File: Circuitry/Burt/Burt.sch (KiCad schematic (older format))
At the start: 50 parts

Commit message: Joe: RTC changed to soic8, added labels to screw terminal, removed shift regs Burt: added shift reg
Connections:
- net labels added: +3.3V, RCLK, SER, SRCLK
- net labels removed: BWL
- wire segments 118 -> 120
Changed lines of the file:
@@
 	1    0    0    -1
 $EndComp
-Text Label 4150 1800 2    50   ~ 0
-BWL
+Text Label 4675 1225 2    50   ~ 0
+IN1
+Text Label 4675 1325 2    50   ~ 0
+IN2
 Text Label 4550 4450 2    50   ~ 0
-BWL
-Text Label 4150 1900 2    50   ~ 0
-IN1
-Text Label 4150 2000 2    50   ~ 0
-IN2
+SER
+Text Label 4550 4650 2    50   ~ 0
+SRCLK
+Text Label 4550 4950 2    50   ~ 0
+RCLK
+Text Label 5350 4450 0    50   ~ 0
+BL1
+Text Label 5350 4550 0    50   ~ 0
+BL1
+Text Label 5350 4650 0    50   ~ 0
+BL1
+Text Label 5350 4750 0    50   ~ 0
+BL1
+Text Label 5350 4850 0    50   ~ 0
+BL1
+Text Label 5350 4950 0    50   ~ 0
+BL1
+Text Label 5350 5050 0    50   ~ 0
+BL1
+Text Label 5350 5150 0    50   ~ 0
+BL1
+$Comp
+L power:GND #PWR?
+U 1 1 5D2A6513
+P 4175 5050
+F 0 "#PWR?" H 4175 4800 50  0001 C CNN
+F 1 "GND" H 4180 4877 50  0000 C CNN
+F 2 "" H 4175 5050 50  0001 C CNN
+F 3 "" H 4175 5050 50  0001 C CNN
+	1    4175 5050
+	1    0    0    -1
+$EndComp
+Wire Wire Line
+	4175 5050 4550 5050
+Wire Wire Line
+	4175 4750 4550 4750
+$Comp
+L power:+3.3V #PWR?
+U 1 1 5D2BCF22
+P 4175 4750
+F 0 "#PWR?" H 4175 4600 50  0001 C CNN
+F 1 "+3.3V" H 4190 4923 50  0000 C CNN
+F 2 "" H 4175 4750 50  0001 C CNN
+F 3 "" H 4175 4750 50  0001 C CNN
+	1    4175 4750
+	1    0    0    -1
+$EndComp
 $EndSCHEMATC

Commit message: Added part URLs
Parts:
- removed D? (x3): LED, symbol Device:LED
- removed D?: D, symbol Device:D
- removed J?: Conn_01x05_Female, symbol Connector:Conn_01x05_Female
- removed Q? (x10): Q_NMOS_DGS, symbol Device:Q_NMOS_DGS
- removed R? (x3): R, symbol Device:R
- added D1: LED, symbol Device:LED
- added Q1, Q2, Q3, Q4, Q5: SSM6N58NU, symbol Custom:SSM6N58NU
- BT1: renamed from BT?; Part URL (none) -> https://www.digikey.com/product-detail/en/jst-sales-america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
- C1, C2: renamed from C?; Part URL (none) -> https://www.digikey.com/product-detail/en/samsung-electro-m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
- M1: renamed from M?; Part URL (none) -> https://www.pololu.com/product/4790/
- R10, R11, R12, R18, R19, R20, R21, R22, R4, R5, R8, R9: renamed from R?; Part URL (none) -> https://www.digikey.com/product-detail/en/yageo/RT0603BRD07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
- R6, R7: renamed from R?; Part URL (none) -> https://www.digikey.com/product-detail/en/yageo/RC0603FR-07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
- U1, U3: renamed from U?; Part URL (none) -> https://www.digikey.com/product-detail/en/microchip-technol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
- U2: renamed from U?; Part URL (none) -> https://www.digikey.com/product-detail/en/allegro-microsyst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
- U4: renamed from U?; Part URL (none) -> https://www.digikey.com/product-detail/en/nexperia-usa-inc/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
- gave numbers to parts that had none: 10
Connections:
- wire segments 120 -> 117
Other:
- note removed: "Programming LEDs"

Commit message: burt organization and screw terminal and image sensor connector
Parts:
- added J?: Conn_01x08_Female, symbol Connector:Conn_01x08_Female
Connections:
- net labels added: +3V3, CS, MISO, MOSI, SCL, SCLK, SDA
- net labels removed: +3.3V, RX, TX
- wire segments 117 -> 116
- no-connect marks 0 -> 1
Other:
- note added: "Burn Wire Circuitry for Launchers"
- note added: "Burn Wire Circuitry for Pyrolysis"
- note added: "Burn Wire Input 1 for Pyrolysis"
- note added: "Burn Wire Input 2 for Pyrolysis"
- note added: "CS Input for Img Sensor"
- note added: "Img Sensor Data Output"
- note added: "Input = Data from Burt to Joe\nOutput = Data from Joe to Burt"
- note added: "MISO Input for Img Sensor"
- note added: "MOSI Input for Img Sensor"
- note added: "Motor Driver for Launchers Input 1"
- note added: "Motor Driver for Launchers Input 2"
- note added: "Reg Clk Input for Shift Reg"
- note added: "SCL Input for Img Sensor"
- note added: "SCLK Input for Img Sensor"
- note added: "SDA Input for Img Sensor"
- note added: "Serial Clk Input for Shift Reg"
- note added: "Serial Input for Shift Reg"
- note added: "Temp Sensor Data Output"
- note removed: "Burt <--> Joe"
- moved on the sheet: BT1, C1, C2, D1, M1, Q1A, Q1B, Q2A, Q2B, Q3A, Q3B, Q4A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

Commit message: fixed burn wire circuits
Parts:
- removed unit 2 of Q1
- removed Q2, Q3, Q4, Q5: SSM6N58NU, symbol Custom:SSM6N58NU
- removed R10, R11, R12, R18, R19, R20, R21, R22, R9: 10k, symbol Device:R
- removed R14, R15, R16, R17, R23, R24, R25, R26, R27: BURNWIRE, symbol Device:R
- added J?: Conn_01x17, symbol Connector_Generic:Conn_01x17
- added Q? (x9): SSM6N58NU, symbol Custom:SSM6N58NU
- added R? (x9): BURNWIRE, symbol Device:R
- added R? (x9): 10k, symbol Device:R
- J?: Part URL (none) -> https://www.digikey.com/product-detail/en/sullins-connector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
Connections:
- net labels added: CS_IMG, SCK
- net labels removed: CVBS
- wire segments 116 -> 86
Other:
- note added: "Drain"
- note added: "Gate\n"
- note added: "Shift Registers for Launcher Burn Wires"
- note added: "Source"
- note removed: "Img Sensor Data Output"
- moved on the sheet: Q1A, R13, R8, U4

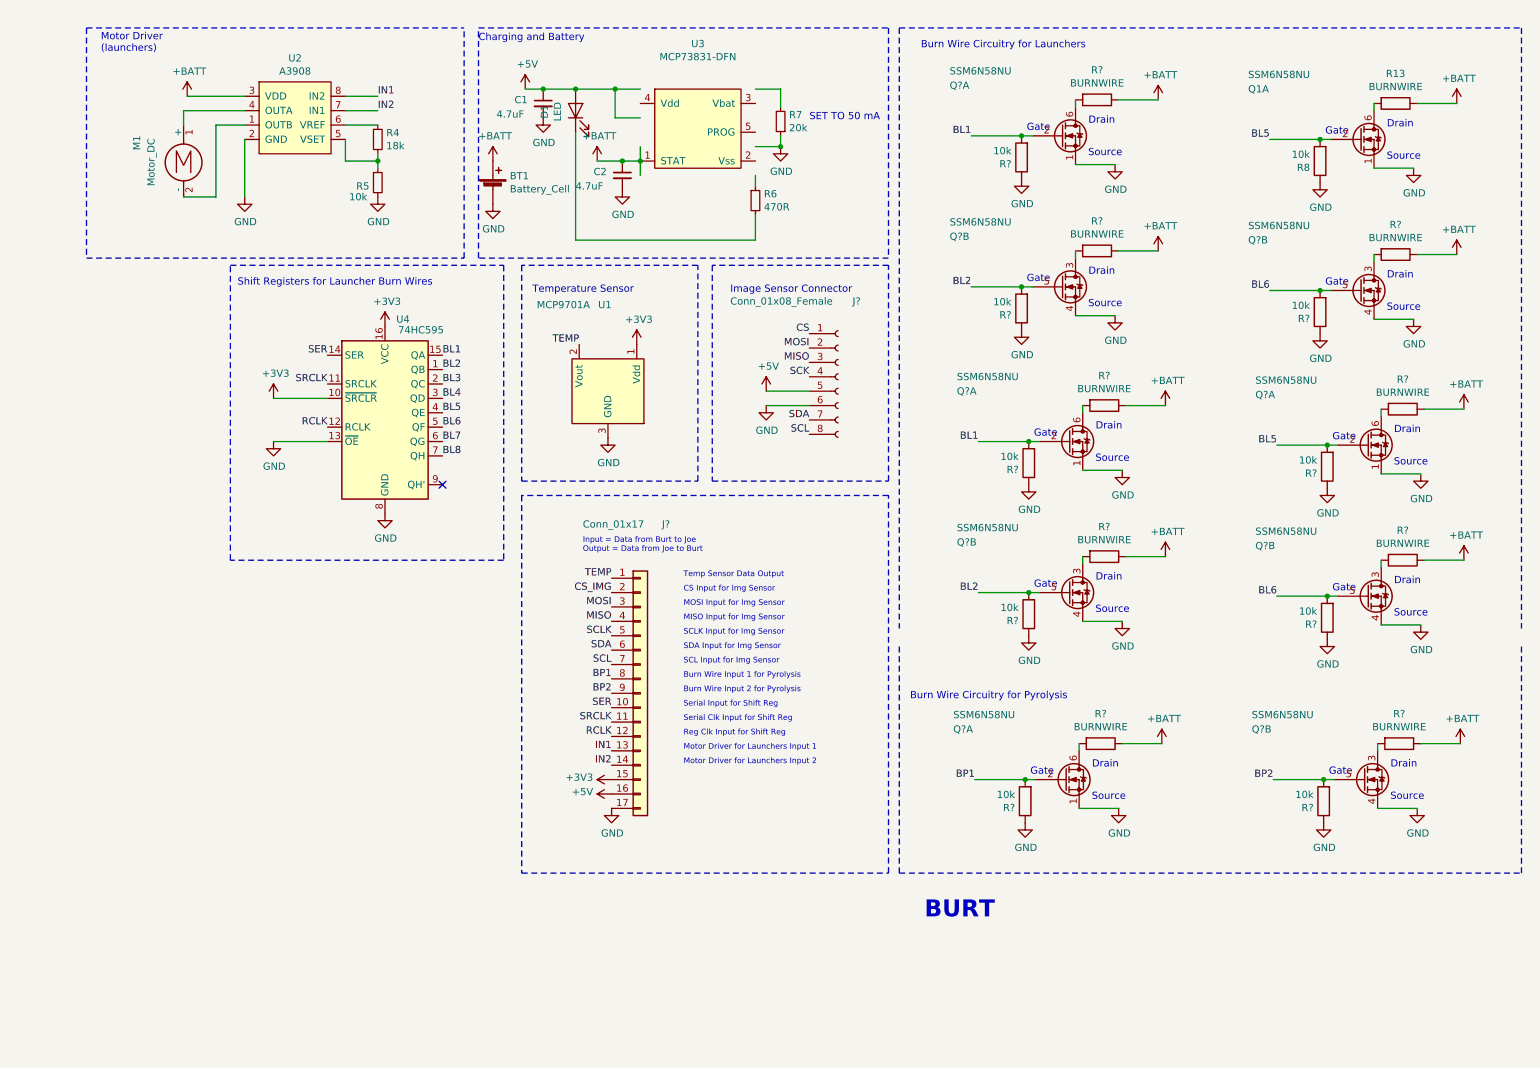
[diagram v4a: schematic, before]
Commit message: electrical rules check ran and corrected
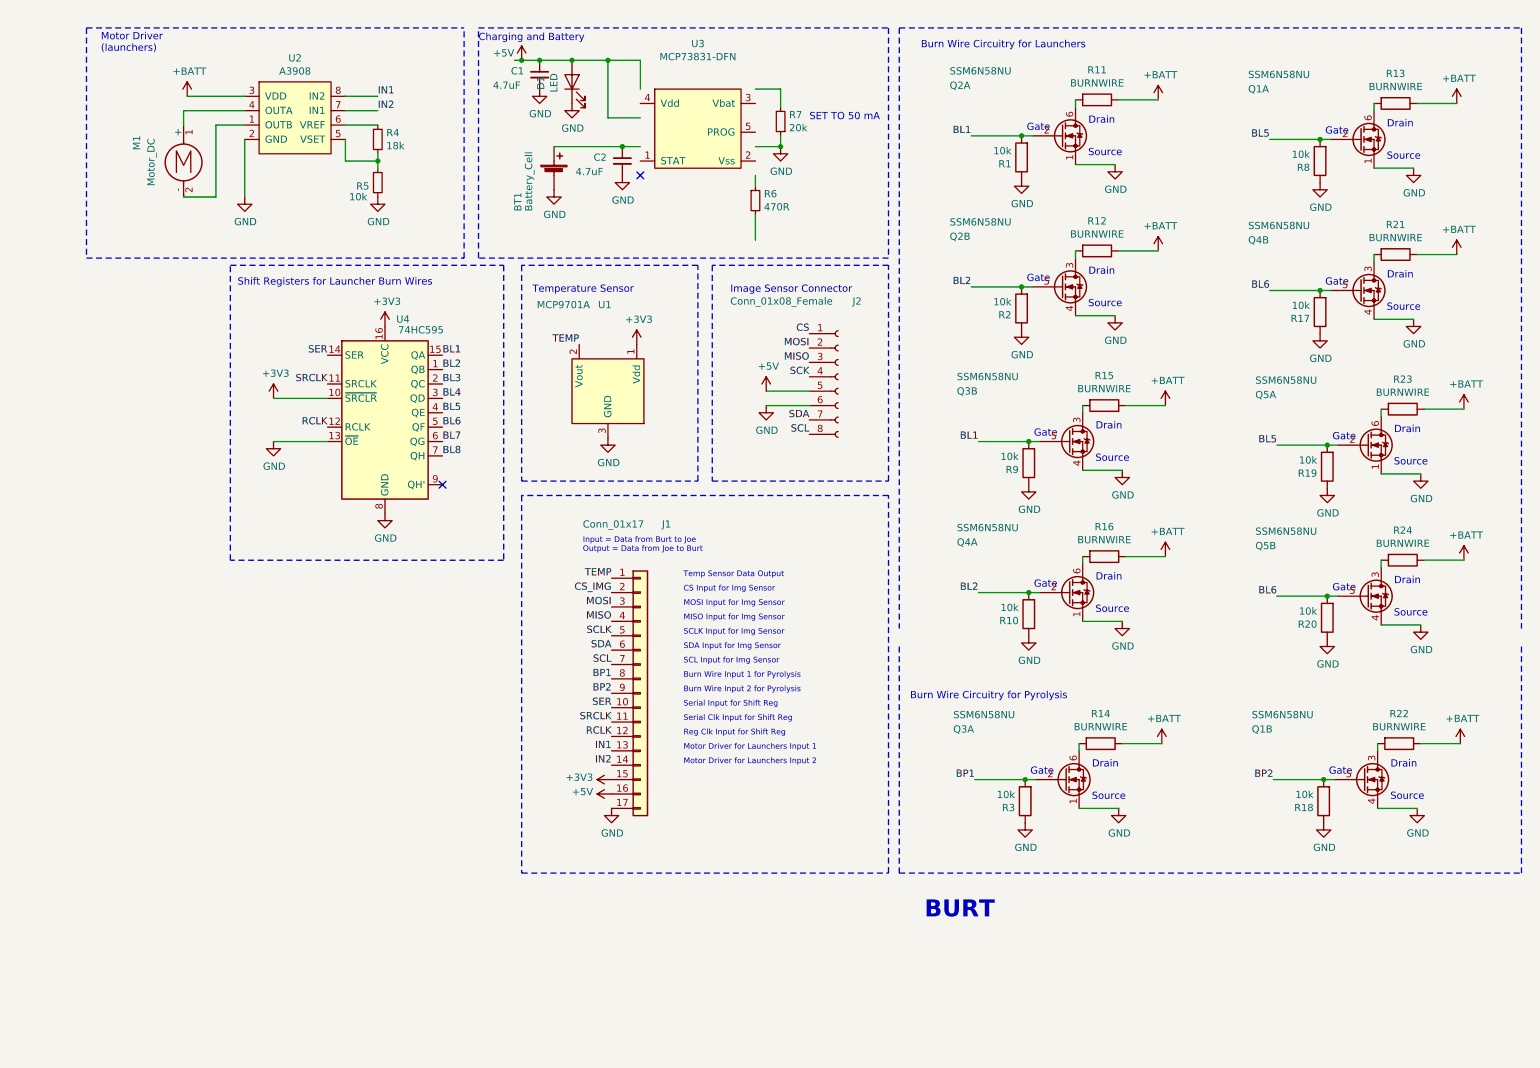
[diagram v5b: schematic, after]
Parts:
- gave numbers to parts that had none: 25
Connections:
- wire segments 86 -> 84
- no-connect marks 1 -> 2
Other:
- moved on the sheet: BT1, C1, C2, D1

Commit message: footprints for burt
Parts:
- C1, C2: footprint (none) -> Capacitor_SMD:C_0603_1608Metric
- D1: footprint (none) -> LED_SMD:LED_0201_0603Metric
- J2: footprint (none) -> Connector_PinSocket_1.00mm:PinSocket_1x08_P1.00mm_Vertical
- M1: footprint (none) -> Connector_JST:JST_JWPF_B02B-JWPF-SK-R_1x02_P2.00mm_Vertical
- Q1, Q2, Q3, Q4, Q5: footprint (none) -> Package_DFN_QFN:DFN-6-1EP_2x2mm_P0.65mm_EP1x1.6mm
- R1, R10, R17, R18, R19, R2, R20, R3, R4, R5, R6, R7, R8, R9: footprint (none) -> Resistor_SMD:R_0603_1608Metric
- R11, R12, R13, R14, R15, R16, R21, R22, R23, R24: footprint (none) -> Connector_PinHeader_1.00mm:PinHeader_1x02_P1.00mm_Vertical
- U1: footprint (none) -> Package_TO_SOT_SMD:SOT-23
- U2: footprint (none) -> Custom:A3908
- U3: footprint (none) -> Package_DFN_QFN:DFN-8-1EP_3x2mm_P0.5mm_EP1.3x1.5mm

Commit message: Fixed some garbage
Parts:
- BT1: footprint (none) -> Connector_JST:JST_PH_B2B-PH-K_1x02_P2.00mm_Vertical
- D1: footprint LED_SMD:LED_0201_0603Metric -> LED_SMD:LED_0603_1608Metric
- J1: footprint (none) -> Custom:0522071733
- J2: footprint Connector_PinSocket_1.00mm:PinSocket_1x08_P1.00mm_Vertical -> Connector_PinHeader_2.54mm:PinHeader_1x08_P2.54mm_Vertical
- M1: footprint Connector_JST:JST_JWPF_B02B-JWPF-SK-R_1x02_P2.00mm_Vertical -> Connector_JST:JST_PH_B2B-PH-K_1x02_P2.00mm_Vertical
- U3: footprint Package_DFN_QFN:DFN-8-1EP_3x2mm_P0.5mm_EP1.3x1.5mm -> Package_TO_SOT_SMD:SOT-23-5; Part URL https://www.digikey.com/product-detail/en/microchip-technology/MCP73831T-2ACI-MC/MCP73831T-2ACI-MCCT-ND/7065590 -> https://www.digikey.com/product-detail/en/microchip-technology/MCP73831T-2ACI-OT/MCP73831T-2ACI-OTCT-ND/1979802
- U4: footprint (none) -> Package_SO:SOIC-16_3.9x9.9mm_P1.27mm
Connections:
- wire segments 84 -> 82
- no-connect marks 2 -> 1
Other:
- moved on the sheet: BT1, C2, R6, R7
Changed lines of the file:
@@
 L Device:R_Small R6
 U 1 1 5D28D225
-P 5825 1750
-F 0 "R6" H 5884 1796 50  0000 L CNN
-F 1 "470R" H 5884 1705 50  0000 L CNN
-F 2 "Resistor_SMD:R_0603_1608Metric" H 5825 1750 50  0001 C CNN
-F 3 "~" H 5825 1750 50  0001 C CNN
-F 4 "https://www.digikey.com/product-detail/en/yageo/RC0603FR-07470RL/311-470HRCT-ND/730203" H 5825 1750 50  0001 C CNN "Part URL"
-	1    5825 1750
+P 4550 1175
+F 0 "R6" H 4609 1221 50  0000 L CNN
+F 1 "470R" H 4609 1130 50  0000 L CNN
+F 2 "Resistor_SMD:R_0603_1608Metric" H 4550 1175 50  0001 C CNN
+F 3 "~" H 4550 1175 50  0001 C CNN
+F 4 "https://www.digikey.com/product-detail/en/yageo/RC0603FR-07470RL/311-470HRCT-ND/730203" H 4550 1175 50  0001 C CNN "Part URL"
+	1    4550 1175
 	1    0    0    -1
 $EndComp
@@
 L Device:R_Small R7
 U 1 1 5D28D9E9
-P 6000 1200
-F 0 "R7" H 5941 1154 50  0000 R CNN
-F 1 "20k" H 5941 1245 50  0000 R CNN
-F 2 "Resistor_SMD:R_0603_1608Metric" H 6000 1200 50  0001 C CNN
-F 3 "~" H 6000 1200 50  0001 C CNN
-F 4 "https://www.digikey.com/product-detail/en/yageo/RC0603FR-0720KL/311-20.0KHRCT-ND/729987" H 6000 1200 50  0001 C CNN "Part URL"
-	1    6000 1200
+P 5925 1375
+F 0 "R7" H 5866 1329 50  0000 R CNN
+F 1 "20k" H 5866 1420 50  0000 R CNN
+F 2 "Resistor_SMD:R_0603_1608Metric" H 5925 1375 50  0001 C CNN
+F 3 "~" H 5925 1375 50  0001 C CNN
+F 4 "https://www.digikey.com/product-detail/en/yageo/RC0603FR-0720KL/311-20.0KHRCT-ND/729987" H 5925 1375 50  0001 C CNN "Part URL"
+	1    5925 1375
 	-1   0    0    1
 $EndComp
-Wire Wire Line
-	5825 975  6000 975
-Wire Wire Line
-	6000 975  6000 1100
-Wire Wire Line
-	5825 1375 6000 1375
-Wire Wire Line
-	6000 1375 6000 1300
 $Comp
 L power:GND #PWR013
 U 1 1 5D292366
-P 6000 1375
-F 0 "#PWR013" H 6000 1125 50  0001 C CNN
-F 1 "GND" H 6005 1202 50  0000 C CNN
-F 2 "" H 6000 1375 50  0001 C CNN
-F 3 "" H 6000 1375 50  0001 C CNN
-	1    6000 1375
-	1    0    0    -1
-$EndComp
-Connection ~ 6000 1375
-Wire Wire Line
-	5825 1575 5825 1650
-Wire Wire Line
-	5825 2025 5825 1850
+P 5925 1525
+F 0 "#PWR013" H 5925 1275 50  0001 C CNN
+F 1 "GND" H 5930 1352 50  0000 C CNN
+F 2 "" H 5925 1525 50  0001 C CNN
+F 3 "" H 5925 1525 50  0001 C CNN
+	1    5925 1525
+	1    0    0    -1
+$EndComp
 Text Label 4825 5075 2    50   ~ 0
 BP1
@@
 Text Label 9400 1325 2    50   ~ 0
 BL5
-Wire Wire Line
-	5025 1375 4900 1375
 $Comp
 L Burt-rescue:A3908-Custom U2
@@
 F 0 "M1" V 1525 1450 50  0000 L CNN
 F 1 "Motor_DC" V 1625 1200 50  0000 L CNN
-F 2 "Connector_JST:JST_JWPF_B02B-JWPF-SK-R_1x02_P2.00mm_Vertical" H 1850 1335 50  0001 C CNN
+F 2 "Connector_JST:JST_PH_B2B-PH-K_1x02_P2.00mm_Vertical" H 1850 1335 50  0001 C CNN
 F 3 "~" H 1850 1335 50  0001 C CNN
 F 4 "https://www.pololu.com/product/4790/" H 1850 1425 50  0001 C CNN "Part URL"
@@
 F 0 "U3" H 5425 1890 50  0000 C CNN
 F 1 "MCP73831-DFN" H 5425 1799 50  0000 C CNN
-F 2 "Package_DFN_QFN:DFN-8-1EP_3x2mm_P0.5mm_EP1.3x1.5mm" H 5425 1275 50  0001 C CNN
+F 2 "Package_TO_SOT_SMD:SOT-23-5" H 5425 1275 50  0001 C CNN
 F 3 "" H 5425 1275 50  0001 C CNN
-F 4 "https://www.digikey.com/product-detail/en/microchip-technology/MCP73831T-2ACI-MC/MCP73831T-2ACI-MCCT-ND/7065590" H 5425 1275 50  0001 C CNN "Part URL"
+F 4 "https://www.digikey.com/product-detail/en/microchip-technology/MCP73831T-2ACI-OT/MCP73831T-2ACI-OTCT-ND/1979802" H 5425 1275 50  0001 C CNN "Part URL"
 	1    5425 1275
 	1    0    0    -1
@@
 L Device:C_Small C2
 U 1 1 5D28C167
-P 4900 1475
-F 0 "C2" H 4700 1500 50  0000 L CNN
-F 1 "4.7uF" H 4575 1400 50  0000 L CNN
-F 2 "Capacitor_SMD:C_0603_1608Metric" H 4900 1475 50  0001 C CNN
-F 3 "~" H 4900 1475 50  0001 C CNN
-F 4 "https://www.digikey.com/product-detail/en/samsung-electro-mechanics/CL10A475MQ8NNNC/1276-1907-1-ND/3889993" H 4900 1475 50  0001 C CNN "Part URL"
-	1    4900 1475
-	1    0    0    -1
-$EndComp
-Connection ~ 4900 1375
-$Comp
-L power:GND #PWR09
-U 1 1 5D28CAB7
-P 4900 1575
-F 0 "#PWR09" H 4900 1325 50  0001 C CNN
-F 1 "GND" H 4905 1402 50  0000 C CNN
-F 2 "" H 4900 1575 50  0001 C CNN
-F 3 "" H 4900 1575 50  0001 C CNN
-	1    4900 1575
-	1    0    0    -1
-$EndComp
-Text Notes 6200 1200 0    50   ~ 0
+P 6225 1175
+F 0 "C2" H 6025 1200 50  0000 L CNN
+F 1 "4.7uF" H 5900 1100 50  0000 L CNN
+F 2 "Capacitor_SMD:C_0603_1608Metric" H 6225 1175 50  0001 C CNN
+F 3 "~" H 6225 1175 50  0001 C CNN
+F 4 "https://www.digikey.com/product-detail/en/samsung-electro-mechanics/CL10A475MQ8NNNC/1276-1907-1-ND/3889993" H 6225 1175 50  0001 C CNN "Part URL"
+	1    6225 1175
+	1    0    0    -1
+$EndComp
+Text Notes 6000 1600 0    50   ~ 0
 SET TO 50 mA
-$Comp
-L Device:Battery_Cell BT1
-U 1 1 5D28E83B
-P 4425 1575
-F 0 "BT1" V 4175 1325 50  0000 L CNN
-F 1 "Battery_Cell" V 4250 1325 50  0000 L CNN
-F 2 "" V 4425 1635 50  0001 C CNN
-F 3 "~" V 4425 1635 50  0001 C CNN
-F 4 "https://www.digikey.com/product-detail/en/jst-sales-america-inc/B2B-PH-K-S-LF-SN/455-1704-ND/926611" H 4425 1575 50  0001 C CNN "Part URL"
-	1    4425 1575
-	1    0    0    -1
-$EndComp
 $Comp
 L power:GND #PWR02
 U 1 1 5D291472
-P 4425 1675
-F 0 "#PWR02" H 4425 1425 50  0001 C CNN
-F 1 "GND" H 4430 1502 50  0000 C CNN
-F 2 "" H 4425 1675 50  0001 C CNN
-F 3 "" H 4425 1675 50  0001 C CNN
-	1    4425 1675
+P 6325 1375
+F 0 "#PWR02" H 6325 1125 50  0001 C CNN
+F 1 "GND" H 6450 1300 50  0000 C CNN
+F 2 "" H 6325 1375 50  0001 C CNN
+F 3 "" H 6325 1375 50  0001 C CNN
+	1    6325 1375
 	1    0    0    -1
 $EndComp
@@
 F 0 "U4" H 3375 3875 50  0000 C CNN
 F 1 "74HC595" H 3500 3800 50  0000 C CNN
-F 2 "" H 3250 3225 50  0001 C CNN
+F 2 "Package_SO:SOIC-16_3.9x9.9mm_P1.27mm" H 3250 3225 50  0001 C CNN
 F 3 "http://www.ti.com/lit/ds/symlink/sn74hc595.pdf" H 3250 3225 50  0001 C CNN
 F 4 "https://www.digikey.com/product-detail/en/nexperia-usa-inc/74HC595D118/1727-2821-1-ND/763394" H 3250 3225 50  0001 C CNN "Part URL"
@@
 F 0 "J2" H 6500 3500 50  0000 L CNN
 F 1 "Conn_01x08_Female" H 5650 3500 50  0000 L CNN
-F 2 "Connector_PinSocket_1.00mm:PinSocket_1x08_P1.00mm_Vertical" H 6400 2975 50  0001 C CNN
+F 2 "Connector_PinHeader_2.54mm:PinHeader_1x08_P2.54mm_Vertical" H 6400 2975 50  0001 C CNN
 F 3 "~" H 6400 2975 50  0001 C CNN
 F 4 "https://www.digikey.com/product-detail/en/sullins-connector-solutions/PPTC081LGBN-RC/S5444-ND/775902" H 6400 2975 50  0001 C CNN "Part URL"
@@
 F 0 "J1" H 5175 6350 50  0000 L CNN
 F 1 "Conn_01x17" H 4625 6350 50  0000 L CNN
-F 2 "" H 5025 5175 50  0001 C CNN
+F 2 "Custom:0522071733" H 5025 5175 50  0001 C CNN
 F 3 "~" H 5025 5175 50  0001 C CNN
 F 4 "https://www.digikey.com/product-detail/en/molex/0522071733/WM10952CT-ND/5170967" H 5025 5175 50  0001 C CNN "Part URL"
@@
 	9425 5775 9775 5775
 Connection ~ 9775 5775
-Wire Wire Line
-	4425 1375 4900 1375
-NoConn ~ 5025 1575
 $Comp
 L Device:LED D1
@@
 F 0 "D1" H 4543 1141 50  0000 C CNN
 F 1 "LED" H 4543 1050 50  0000 C CNN
-F 2 "LED_SMD:LED_0201_0603Metric" H 4550 925 50  0001 C CNN
+F 2 "LED_SMD:LED_0603_1608Metric" H 4550 925 50  0001 C CNN
 F 3 "~" H 4550 925 50  0001 C CNN
 F 4 "https://www.digikey.com/product-detail/en/lumex-opto-components-inc/SML-LXFM0603SUGCTR/67-2320-1-ND/9521881" H 4550 925 50  0001 C CNN "Part URL"
@@
 $EndComp
 Wire Wire Line
-	4550 775  4800 775
-Wire Wire Line
-	5025 775  5025 975
+	5025 775  5025 1075
 Connection ~ 4550 775
-Wire Wire Line
-	4800 775  4800 1175
-Wire Wire Line
-	4800 1175 5025 1175
-Connection ~ 4800 775
-Wire Wire Line
-	4800 775  5025 775
-$Comp
-L power:GND #PWR0140
-U 1 1 5D9A62EB
-P 4550 1075
-F 0 "#PWR0140" H 4550 825 50  0001 C CNN
-F 1 "GND" H 4555 902 50  0000 C CNN
-F 2 "" H 4550 1075 50  0001 C CNN
-F 3 "" H 4550 1075 50  0001 C CNN
-	1    4550 1075
-	1    0    0    -1
-$EndComp
-Wire Wire Line
-	4200 775  4150 775
-Connection ~ 4200 775
+$Comp
+L Device:Battery_Cell BT1
+U 1 1 5D28E83B
+P 6425 1275
+F 0 "BT1" V 6475 1450 50  0000 L CNN
+F 1 "Battery_Cell" V 6550 1100 50  0000 L CNN
+F 2 "Connector_JST:JST_PH_B2B-PH-K_1x02_P2.00mm_Vertical" V 6425 1335 50  0001 C CNN
+F 3 "~" V 6425 1335 50  0001 C CNN
+F 4 "https://www.digikey.com/product-detail/en/jst-sales-america-inc/B2B-PH-K-S-LF-SN/455-1704-ND/926611" H 6425 1275 50  0001 C CNN "Part URL"
+	1    6425 1275
+	1    0    0    -1
+$EndComp
+Wire Wire Line
+	4550 775  5025 775
+Wire Wire Line
+	4550 1275 4550 1475
+Wire Wire Line
+	4550 1475 5025 1475
+Wire Wire Line
+	5825 1275 5925 1275
+Wire Wire Line
+	5925 1475 5825 1475
+Wire Wire Line
+	5925 1525 5925 1475
+Connection ~ 5925 1475
+Connection ~ 6225 1075
+Wire Wire Line
+	6225 1075 6425 1075
+Wire Wire Line
+	5825 1075 6225 1075
+Wire Wire Line
+	6225 1275 6225 1375
+Wire Wire Line
+	6225 1375 6325 1375
+Wire Wire Line
+	6325 1375 6425 1375
+Connection ~ 6325 1375
 $EndSCHEMATC
